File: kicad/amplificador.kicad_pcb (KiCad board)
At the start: 2 copper layers, 202 x 103 mm, 86 parts, among them J1 Screw_Terminal_01x01, J10 Conn_01x01_Male, J11 Conn_01x01_Male, J12 Conn_01x01_Male, J13 Conn_01x01_Male, J14 Screw_Terminal_01x01, J15 Conn_01x01_Male, J16 Screw_Terminal_01x01, J17 Screw_Terminal_01x01, J18 Conn_01x01_Male, J19 Conn_01x01_Male, J2 Conn_01x01_Male, J20 Conn_01x01_Male, J21 Screw_Terminal_01x01, J22 Screw_Terminal_01x01, J23 Screw_Terminal_01x01, J24 Screw_Terminal_01x01, J3 Conn_01x01_Male, J4 Conn_01x01_Male, J5 Conn_01x01_Male, J6 Conn_01x01_Male, J7 Screw_Terminal_01x01, J8 Screw_Terminal_01x01, J9 Conn_01x01_Male, Q1 MPSA92, Q10 MPSA42, Q11 BD135, Q12 BD136, Q13 BD135, Q14 BD136, Q15 2SD1047, Q16 2SD1047, Q17 2SB817, Q18 2SB817, Q2 MPSA42, Q3 MPSA92, Q4 MPSA42, Q5 MPSA92, Q6 MPSA92, Q7 MPSA42, Q8 MPSA92, Q9 MPSA42, U1 LM385D-1.2, U2 LM385D-1.2

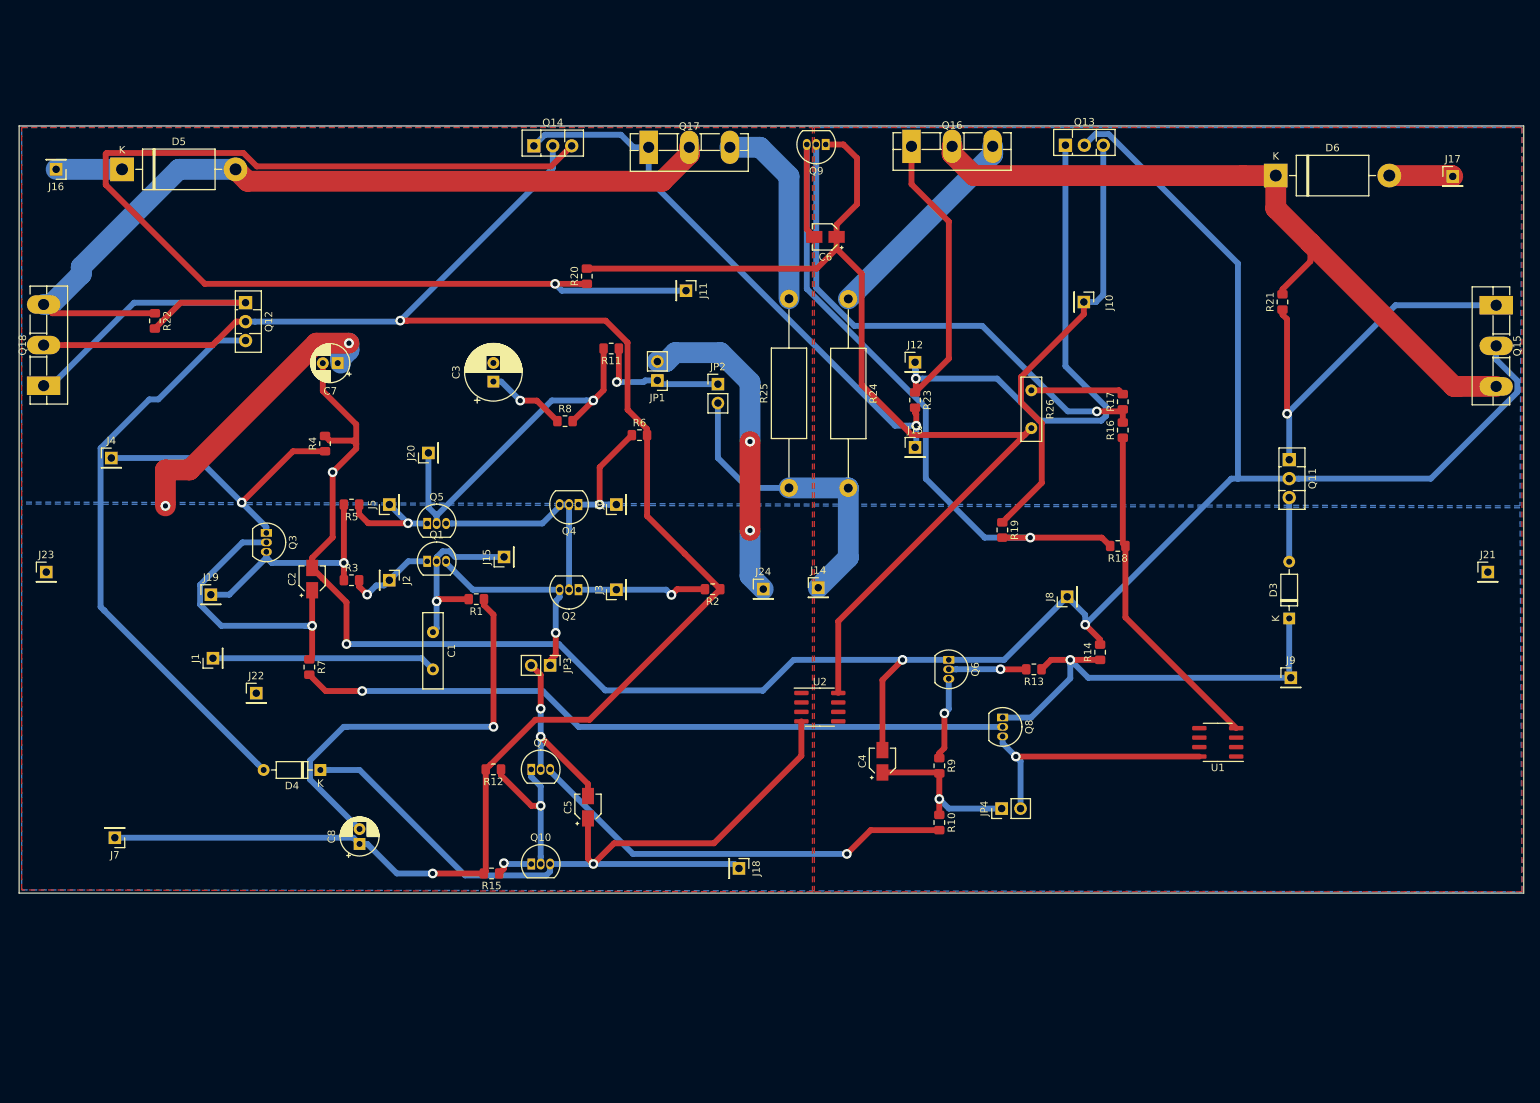
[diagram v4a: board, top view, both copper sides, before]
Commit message: Se cambio el footprint del multiplicador de vbe en el pcb
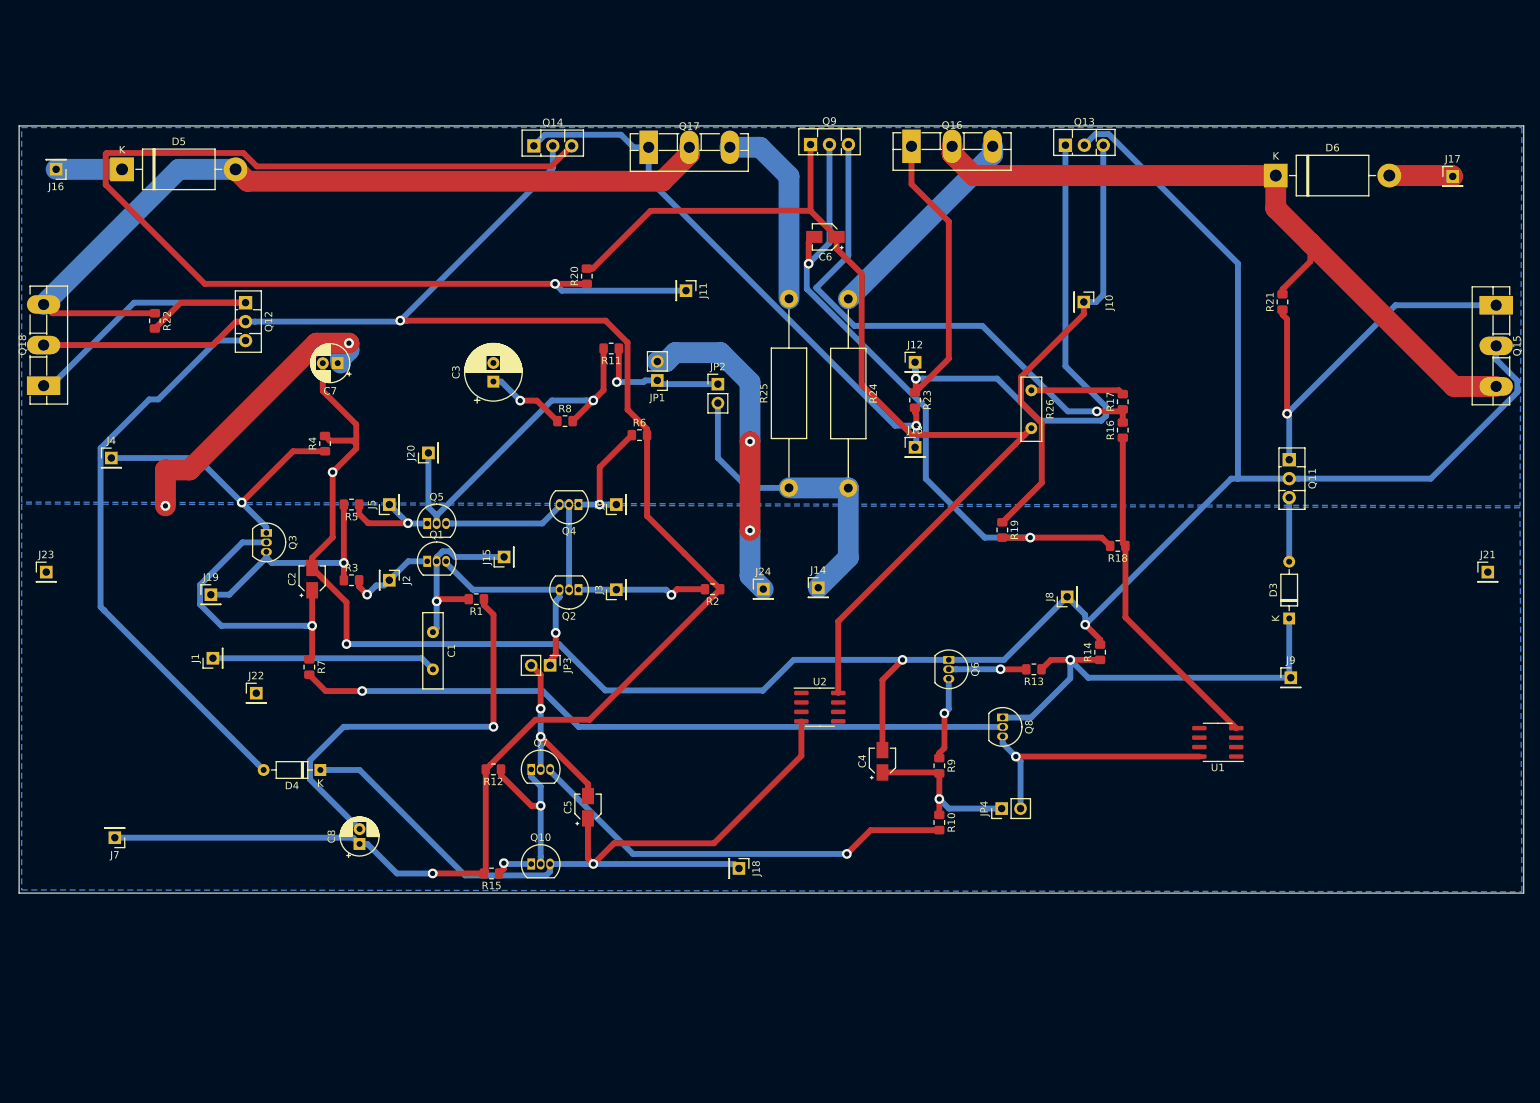
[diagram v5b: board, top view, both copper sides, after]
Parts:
- Q9: value MPSA42 -> BD135; footprint Package_TO_SOT_THT:TO-92_Inline -> Package_TO_SOT_THT:TO-126-3_Vertical
- moved Q9 2.03 mm to (159.3, 31.5), turned to 0 degrees
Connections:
- net Net-(C1-Pad1) renamed /Via
- net Net-(C1-Pad2) renamed /Vi
- net Net-(C2-Pad2) renamed /+Vcc
- net Net-(C5-Pad1) renamed /Vo_vas
- net Net-(C5-Pad2) renamed /Vi_buffer
- net Net-(C8-Pad1) renamed /-Vcc
- net Net-(J14-Pad1) renamed /Vo
- net Net-(J19-Pad1) renamed /Io1
- net Net-(JP3-Pad1) renamed /Vo_sumador
- net Net-(JP4-Pad2) renamed /Io2
- net Net-(Q10-Pad2) renamed /Vi_vas
- Q9 pad 2: Net-(Q9-Pad2) -> Net-(C6-Pad2)
- Q9 pad 3: Net-(C6-Pad2) -> Net-(Q9-Pad3)
- R16 pad 2: Net-(Q9-Pad2) -> Net-(Q9-Pad3)
- R17 pad 1: Net-(Q9-Pad2) -> Net-(Q9-Pad3)
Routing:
- net Net-(Q9-Pad3): track 0.00 -> 70.9 mm, vias 0 -> 1
- net Net-(Q9-Pad2): track 69.1 -> 0.00 mm, vias 1 -> 0
- net Net-(C6-Pad2): track 96.6 -> 88.9 mm, vias 1 -> 2
- net Net-(C6-Pad1): track 144.8 -> 140.6 mm
- net Net-(D5-Pad2): track 113.3 -> 112.7 mm
- removed copper zone on F.Cu, net /-Vcc

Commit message: configurado con un clearance de 0.32 mm
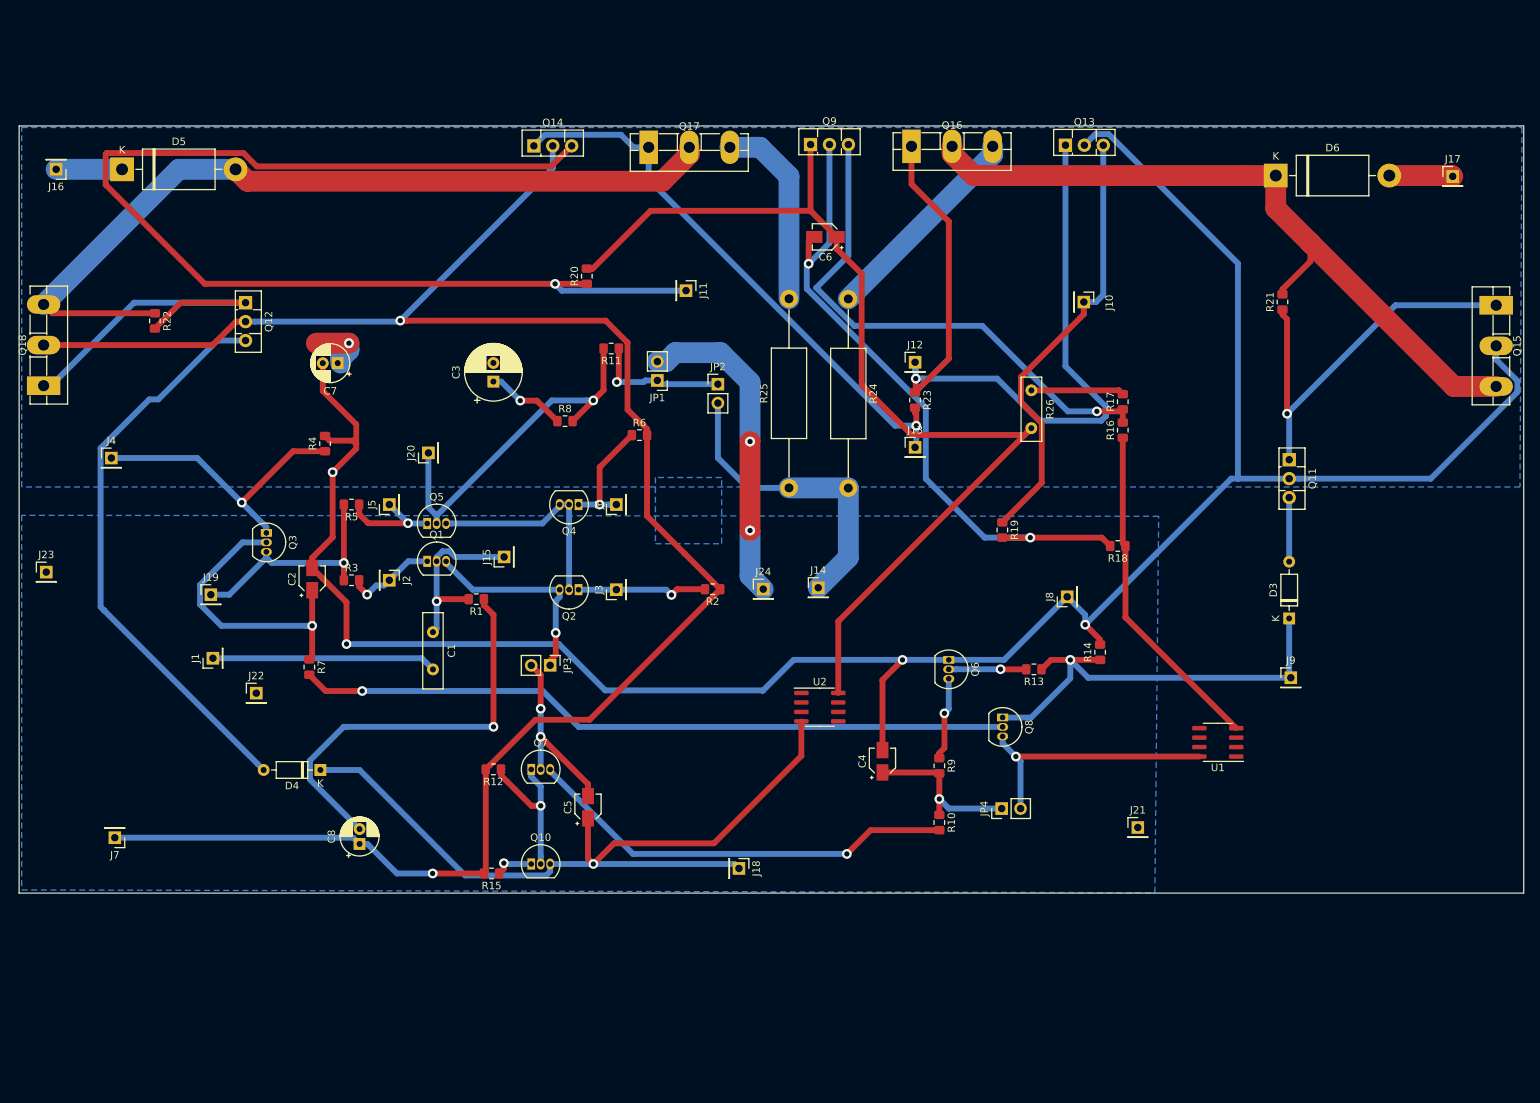
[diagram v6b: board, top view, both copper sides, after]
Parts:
- moved J21 58.2 mm to (203.2, 123.2)
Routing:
- net GND: track 197.3 -> 165.2 mm, vias 6 -> 5
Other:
- net class Default: clearance 0.2 -> 0.32
- rule trace_clearance: 0.2 -> 0.32

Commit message: DRC arreglo - separación pista pad
Problema a resolver: los transistores Q1 a Q10 (MPSA) tienen sus pad muy cercanos entre sí y no cumplen las reglas del LCI. ¿Hay que cambiar de transistores?
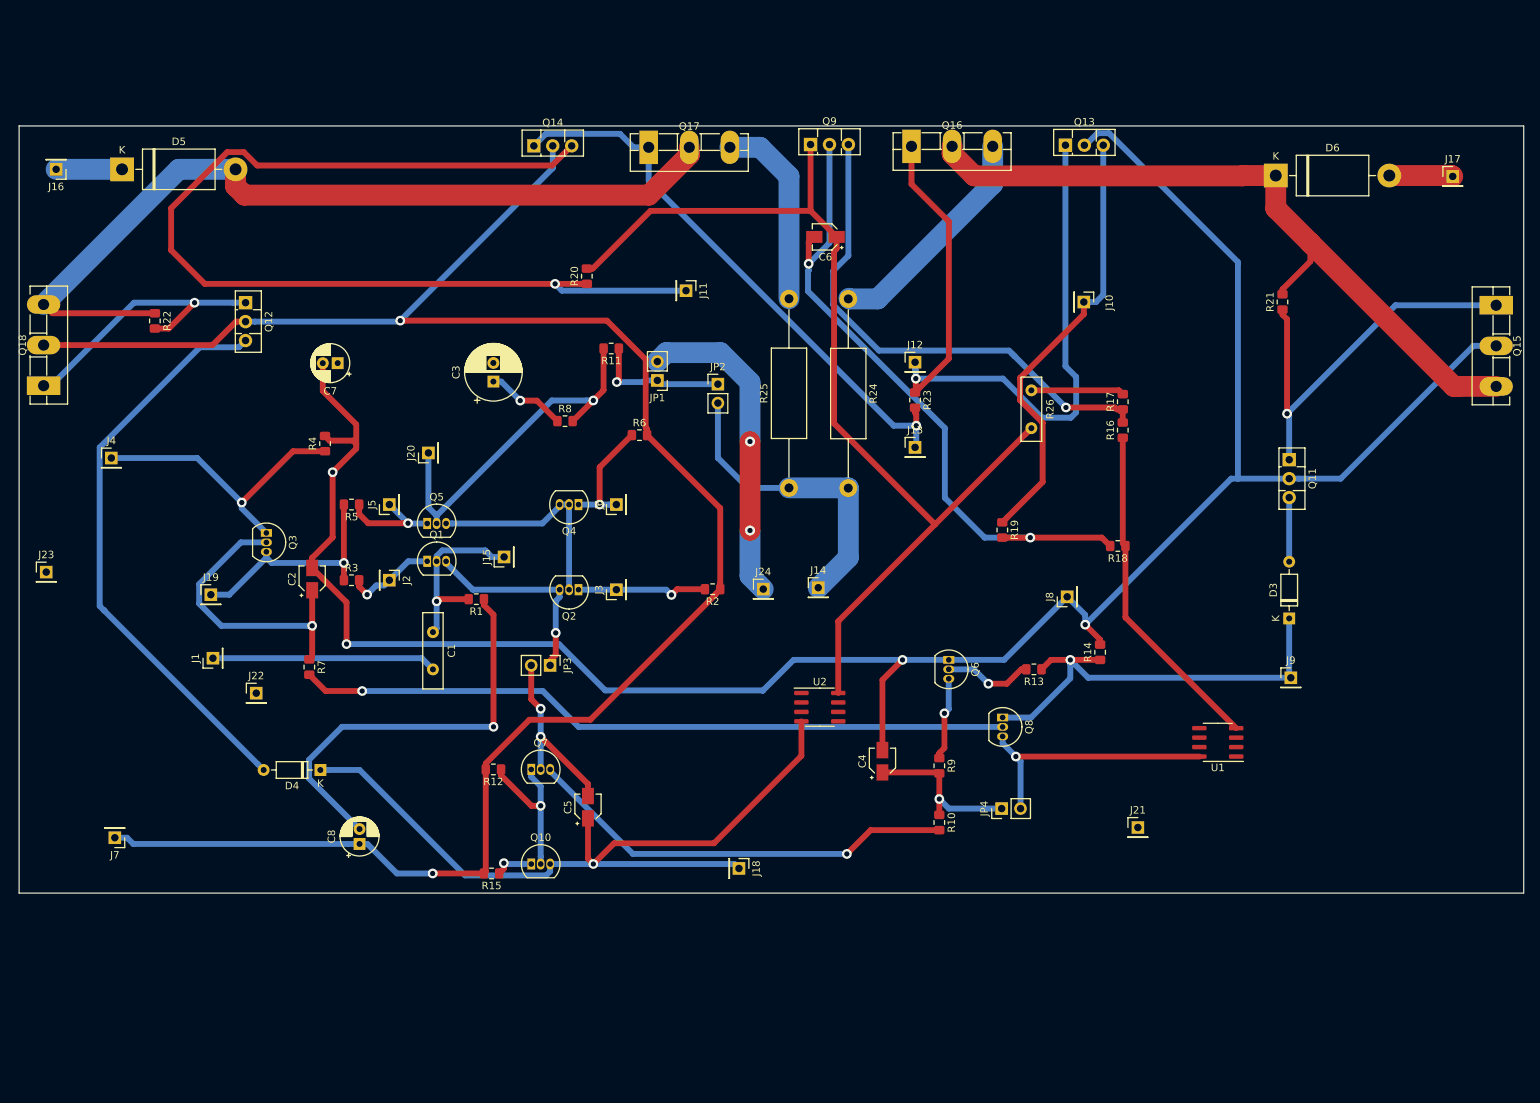
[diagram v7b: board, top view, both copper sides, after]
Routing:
- net Net-(J11-Pad1): track 156.7 -> 140.0 mm
- net /+Vcc: track 310.8 -> 303.4 mm
- net GND: track 165.2 -> 157.9 mm, vias 5 -> 4
- net Net-(Q12-Pad1): track 45.3 -> 38.5 mm, vias 0 -> 1
- net Net-(J12-Pad1): track 107.9 -> 101.6 mm
- net Net-(D5-Pad2): track 112.7 -> 115.6 mm
- net Net-(Q16-Pad3): track 28.5 -> 30.8 mm
- net Net-(Q6-Pad2): track 10.4 -> 12.0 mm
- net Net-(C6-Pad1): track 140.6 -> 139.1 mm
- net /-Vcc: track 259.1 -> 260.5 mm
- net Net-(Q9-Pad3): track 70.9 -> 69.9 mm
- removed copper zone on B.Cu, net GND

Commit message: Planos de masa agregados
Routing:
- net GND: track 157.9 -> 191.3 mm
- added copper zone on B.Cu, net GND
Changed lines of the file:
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@@
     (thickness 1.6)
     (drawings 4)
-    (tracks 495)
+    (tracks 498)
     (zones 0)
     (modules 86)
@@
   (segment (start 151.13 71.374) (end 151.13 71.374) (width 2.799994) (layer B.Cu) (net 3))
   (via (at 151.13 71.374) (size 1.335024) (drill 0.700024) (layers F.Cu B.Cu) (net 3))
-  (segment (start 151.13 71.374) (end 151.13 83.312) (width 2.799994) (layer F.Cu) (net 3))
-  (segment (start 151.13 83.312) (end 151.13 83.312) (width 2.799994) (layer F.Cu) (net 3))
-  (via (at 151.13 83.312) (size 1.335024) (drill 0.700024) (layers F.Cu B.Cu) (net 3))
-  (segment (start 151.13 89.408) (end 152.908 91.186) (width 2.799994) (layer B.Cu) (net 3))
-  (segment (start 151.13 83.312) (end 151.13 89.408) (width 2.799994) (layer B.Cu) (net 3))
+  (segment (start 151.13 89.408) (end 151.13 89.408) (width 2.799994) (layer B.Cu) (net 3))
   (segment (start 164.12972 126.74092) (end 135.41862 126.74092) (width 0.7874) (layer B.Cu) (net 3))
   (segment (start 116.6876 109.67212) (end 116.6876 109.7026) (width 0.7874) (layer F.Cu) (net 3))
@@
   (segment (start 96.358218 109.67212) (end 91.932899 114.097439) (width 0.7874) (layer B.Cu) (net 3))
   (segment (start 116.6876 109.67212) (end 96.358218 109.67212) (width 0.7874) (layer B.Cu) (net 3))
+  (segment (start 151.13 89.408) (end 152.908 91.186) (width 2.799994) (layer B.Cu) (net 3))
+  (via (at 151.13 89.408) (size 1.309624) (drill 0.700024) (layers F.Cu B.Cu) (net 3))
+  (segment (start 151.13 71.374) (end 151.13 89.408) (width 2.799994) (layer F.Cu) (net 3))
+  (segment (start 114.781528 91.908828) (end 115.4049 92.5322) (width 0.7874) (layer F.Cu) (net 3))
+  (segment (start 114.781528 61.584202) (end 114.781528 91.908828) (width 0.7874) (layer F.Cu) (net 3))
+  (segment (start 115.54353 60.8222) (end 114.781528 61.584202) (width 0.7874) (layer F.Cu) (net 3))
+  (segment (start 116.6749 60.8222) (end 115.54353 60.8222) (width 0.7874) (layer F.Cu) (net 3))
   (segment (start 176.5427 115.9256) (end 176.5427 119.3673) (width 0.7874) (layer F.Cu) (net 4))
   (segment (start 176.4171 115.8) (end 176.5427 115.9256) (width 0.7874) (layer F.Cu) (net 4))
@@
   (segment (start 186.69 59.944) (end 193.548 66.802) (width 0.7874) (layer B.Cu) (net 47))
   (segment (start 186.21248 59.46648) (end 186.69 59.944) (width 0.7874) (layer B.Cu) (net 47))
+  (zone (net 3) (net_name GND) (layer B.Cu) (hatch edge 0.508)
+    (connect_pads (clearance 0.508))
+    (min_thickness 0.254)
+    (fill yes (arc_segments 32) (thermal_gap 0.508) (thermal_bridge_width 0.508))
+    (polygon
+      (pts
+        (xy 53.34 29.21) (xy 209.296 29.21) (xy 209.296 80.772) (xy 53.086 80.772)
+      )
+    )
+  )
+  (zone (net 3) (net_name GND) (layer B.Cu) (hatch edge 0.508)
+    (connect_pads (clearance 0.508))
+    (min_thickness 0.254)
+    (fill yes (arc_segments 32) (thermal_gap 0.508) (thermal_bridge_width 0.508))
+    (polygon
+      (pts
+        (xy 53.086 84.074) (xy 214.376 84.074) (xy 214.376 131.826) (xy 53.086 131.826)
+      )
+    )
+  )
 )
